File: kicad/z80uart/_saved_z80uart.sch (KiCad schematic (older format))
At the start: 7 parts, among them U1 16550, U100 serial_port_interface, U101 z80pcb, U2 74LS238, X1 XO-14S

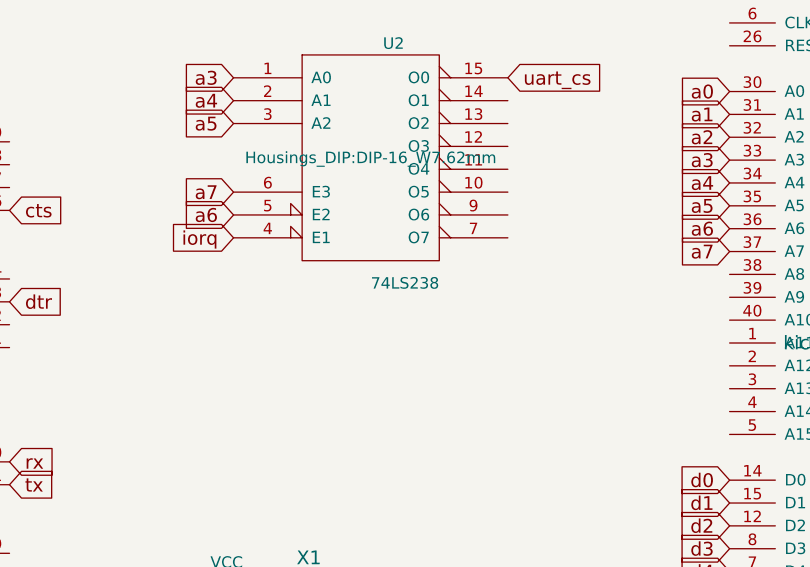
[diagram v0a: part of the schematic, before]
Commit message: add UART board
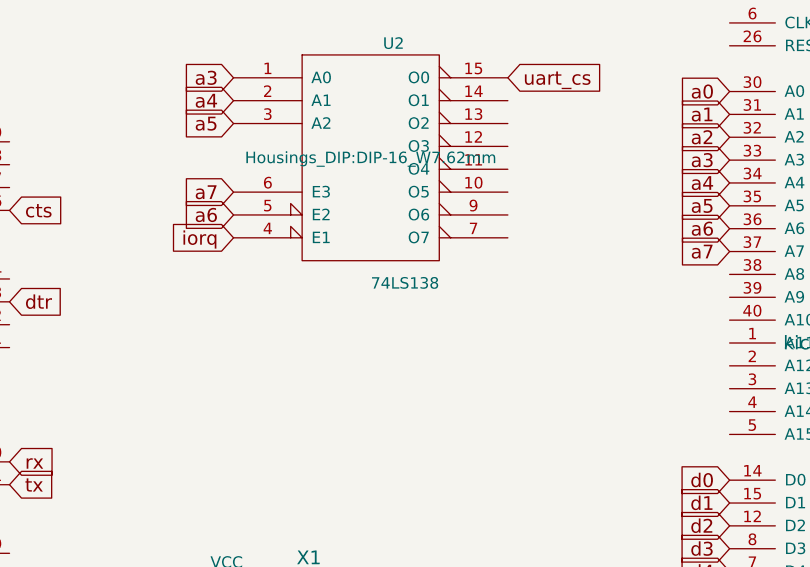
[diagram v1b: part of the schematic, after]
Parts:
- U2: value 74LS238 -> 74LS138
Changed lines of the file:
@@
 P 8580 2630
 F 0 "U2" H 8680 3130 50  0000 C CNN
-F 1 "74LS238" H 8730 2081 50  0000 C CNN
+F 1 "74LS138" H 8730 2081 50  0000 C CNN
 F 2 "Housings_DIP:DIP-16_W7.62mm" H 8580 2630 50  0000 C CNN
 F 3 "" H 8580 2630 50  0000 C CNN
